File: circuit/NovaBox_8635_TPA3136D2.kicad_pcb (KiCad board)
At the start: 2 copper layers, 100 x 100 mm, 99 parts, among them P1 USB, P2 MH, P3 MH, P4 MH, P5 MH, Q1 IRLML6401, Q2 MMBT3904, Q3 IRLML6401, Q4 IRLML6344, Q5 MMBT3904, SW1 PIO18, SW2 PIO21, SW3 PIO8, SW4 PIO0, SW5 PIO1, SW6 ON/OFF, U1 CSR8635_MODULE, U2 CSR_DebugSmall, U3 TPA3136D2, U4 MCP6004

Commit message: mo powah pcb continued
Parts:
- removed C32: 1uF, NovaBox:C_0805
- removed L1, L3: 3.1A, NovaBox:R_0805
- removed SPK_LEFT1, SPK_RIGHT1: SPK, NovaBox:SPKR
- added L5: 3.1A, NovaBox:R_0805, F.Cu at (98.0, 122.0)
- added L6: 3.1A, NovaBox:R_0805, F.Cu at (90.5, 118.5)
- added R5: 10k, NovaBox:R_0805, F.Cu at (81.5, 104.0)
- added SPK1: SPK_L, NovaBox:SPKR, F.Cu at (114.0, 131.8)
- added SPK2: SPK_R, NovaBox:SPKR, F.Cu at (93.5, 132.5)
- C1: value 100uF -> 1uF; footprint NovaBox:CPOL_D10_P4.5 -> NovaBox:C_0805; moved to F.Cu
- C11, C24, C25: value 1nF -> 1uF
- C13, C22, C23, C27, C28, C6: value 1uF -> 1nF
- C14: value 220nF -> 1nF
- C15, C21: value 220nF -> 1uF
- C16: value 100nF -> 1uF
- C17: value 1uF -> 220nF
- C19, C20: value 1nF -> 220nF
- C2, C8: value 100nF -> 100uF; footprint NovaBox:C_0805 -> NovaBox:CPOL_D10_P4.5; moved to B.Cu
- C3, C5, C9: value 1nF -> 100nF
- C7: value 100uF -> 1nF; footprint NovaBox:CPOL_D10_P4.5 -> NovaBox:C_0805; moved to F.Cu
- Q2: value MMBT3904 -> IRLML6401
- Q3: value IRLML6401 -> MMBT3904
- Q4: value IRLML6344 -> MMBT3904
- Q5: value MMBT3904 -> IRLML6344
- R1: value 68 -> 1K
- R10: value 100k -> 10k
- R11: value 240K -> 68
- R12: value 620K -> 240K
- R13: value 68 -> 620K
- R17: value 240K -> 10K
- R18, R24: value 470K -> 10K
- R19: value 750 -> 240K
- R2: value 1K -> 68
- R21: value 270K -> 470K
- R22: value 10K -> 750
- R23: value 1K -> 270K
- R25: value 10K -> 470K
- R27: value 2K -> 1K
- R29: value 10K -> 2K
- R3: value 68 -> 10K
- R4, R8: value 10k -> 68
- R6: value 10K -> 100k; footprint NovaBox:R_0805 -> NovaBox:RPOT_RKT6V; moved to B.Cu
- R9: value 68 -> 100k
- moved C14 128.0 mm to (108.5, 132.0), turned to 180 degrees
- moved C18 127.1 mm to (101.5, 117.5), turned to 180 degrees
- moved C15 119.7 mm to (101.0, 99.5), turned to 270 degrees
- moved U3 116.9 mm to (99.5, 111.0), turned to 270 degrees
- moved R22 112.9 mm to (217.8, 86.8), turned to 180 degrees
- moved C1 112.7 mm to (223.0, 79.5)
- moved D7 107.3 mm to (217.8, 93.4), turned to 180 degrees
- moved C23 103.4 mm to (93.5, 127.5), turned to 270 degrees
- moved R16 102.4 mm to (205.0, 94.5), turned to 0 degrees
- moved C26 101.0 mm to (205.0, 92.5), turned to 0 degrees
- moved R15 101.0 mm to (205.0, 96.5), turned to 0 degrees
- moved C9 100.7 mm to (90.5, 113.5), turned to 270 degrees
- moved R24 98.8 mm to (217.8, 89.0)
- moved C10 98.1 mm to (92.5, 113.5), turned to 270 degrees
- moved R12 97.4 mm to (205.0, 103.5), turned to 0 degrees
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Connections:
- C1 pad 1: +BATT -> GND
- C1 pad 2: GND -> +BATT
- C10 pad 2: Net-(C10-Pad2) -> +BATT
- C11 pad 2: Net-(C10-Pad2) -> Net-(C11-Pad2)
- C12 pad 1: GND -> +5V
- C12 pad 2: Net-(C12-Pad2) -> GND
- C13 pad 1: Net-(C13-Pad1) -> GND
- C14 pad 2: Net-(C14-Pad2) -> Net-(C13-Pad2)
- C16 pad 1: CSR_RST -> GND
- C16 pad 2: GND -> Net-(C16-Pad2)
- C19 pad 1: GND -> Net-(C19-Pad1)
- C2 pad 1: GND -> +BATT
- C2 pad 2: +BATT -> GND
- C20 pad 2: Net-(C19-Pad2) -> Net-(C20-Pad2)
- C21 pad 2: Net-(C21-Pad2) -> GND
- C22 pad 1: Net-(C22-Pad1) -> GND
- C23 pad 2: Net-(C23-Pad2) -> Net-(C22-Pad2)
- C24 pad 1: GND -> Net-(C24-Pad1)
- C25 pad 2: Net-(C24-Pad2) -> Net-(C25-Pad2)
- C27 pad 1: Net-(C27-Pad1) -> GND
- C27 pad 2: GND -> Net-(C27-Pad2)
- C28 pad 2: GND -> Net-(C27-Pad2)
- C29 pad 1: +BATT -> Net-(C29-Pad1)
- C29 pad 2: Net-(C29-Pad2) -> GND
- C31 pad 1: +5V -> +BATT
- C31 pad 2: GND -> Net-(C31-Pad2)
- C4 pad 2: Net-(C4-Pad2) -> +BATT
- C5 pad 1: Net-(C5-Pad1) -> CSR_RST
- C5 pad 2: Net-(C4-Pad2) -> GND
- C6 pad 2: +BATT -> Net-(C6-Pad2)
- C7 pad 1: +BATT -> Net-(C7-Pad1)
- C7 pad 2: GND -> Net-(C6-Pad2)
- C8 pad 1: GND -> +BATT
- C8 pad 2: +BATT -> GND
- L2 pad 1: Net-(C10-Pad2) -> Net-(C6-Pad2)
- L2 pad 2: Net-(C15-Pad1) -> Net-(C17-Pad1)
- L4 pad 1: Net-(C24-Pad2) -> Net-(C13-Pad2)
- L4 pad 2: Net-(C21-Pad1) -> Net-(C18-Pad1)
- Q1 pad 2: GND -> VR_SHDN
- Q1 pad 3: Net-(Q1-Pad3) -> +BATT
- Q2 pad 3: PWER_E -> Net-(Q2-Pad3)
- Q3 pad 2: VR_SHDN -> GND
- Q3 pad 3: +BATT -> Net-(Q1-Pad1)
- Q4 pad 1: +BATT -> Net-(Q4-Pad1)
- Q4 pad 3: Net-(Q4-Pad3) -> PWER_E
- Q5 pad 1: Net-(Q5-Pad1) -> +BATT
- Q5 pad 3: Net-(Q3-Pad1) -> Net-(Q5-Pad3)
- R1 pad 1: Net-(C5-Pad1) -> 1V8
- R1 pad 2: GND -> Net-(R1-Pad2)
- R10 pad 1: Net-(R10-Pad1) -> +BATT
- R10 pad 2: +BATT -> Net-(Q2-Pad1)
- R11 pad 1: Net-(C26-Pad1) -> Net-(C28-Pad1)
- R11 pad 2: +BATT -> GND
- R12 pad 1: Net-(C26-Pad1) -> Net-(C21-Pad1)
- R12 pad 2: GND -> +BATT
- R13 pad 1: Net-(C25-Pad1) -> Net-(C21-Pad1)
- R14 pad 2: Net-(Q1-Pad3) -> Net-(Q2-Pad3)
- R15 pad 1: Net-(C27-Pad1) -> Net-(C26-Pad1)
- R16 pad 1: Net-(C27-Pad1) -> Net-(C26-Pad1)
- R17 pad 1: Net-(C28-Pad1) -> +BATT
- R17 pad 2: +BATT -> Net-(Q1-Pad1)
- R18 pad 1: Net-(C28-Pad1) -> Net-(Q3-Pad1)
- R18 pad 2: GND -> 1V8
- R19 pad 1: 2V5 -> Net-(C29-Pad1)
- R2 pad 1: 1V8 -> Net-(C7-Pad1)
- R2 pad 2: Net-(R2-Pad2) -> GND
- R20 pad 1: PWER_E -> VR_SHDN
- R20 pad 2: +BATT -> GND
- R21 pad 1: Net-(C30-Pad1) -> Net-(C29-Pad1)
- R21 pad 2: +BATT -> GND
- R22 pad 1: GND -> 2V5
- R22 pad 2: 2V5 -> +BATT
- R23 pad 1: Net-(Q2-Pad1) -> Net-(C30-Pad1)
- R23 pad 2: Net-(C29-Pad2) -> +BATT
- R24 pad 1: Net-(C30-Pad1) -> GND
- R24 pad 2: GND -> 2V5
- R25 pad 1: GND -> Net-(C30-Pad1)
- R25 pad 2: Net-(Q2-Pad1) -> GND
- R26 pad 1: +BATT -> PWER_E
- R26 pad 2: Net-(Q3-Pad1) -> +BATT
- R27 pad 1: Net-(Q4-Pad3) -> Net-(Q4-Pad1)
- R27 pad 2: Net-(D8-Pad2) -> Net-(C31-Pad2)
- R28 pad 1: Net-(Q5-Pad1) -> GND
- R28 pad 2: 1V8 -> Net-(Q4-Pad1)
- R29 pad 1: VR_SHDN -> Net-(Q5-Pad3)
- R29 pad 2: GND -> Net-(D8-Pad2)
- R3 pad 1: Net-(C11-Pad1) -> 1V8
- R3 pad 2: GND -> SPI_PCM
- R4 pad 1: (no net) -> Net-(C14-Pad1)
- R6 pad 1: 1V8 -> Net-(C16-Pad2)
- R6 pad 2: SPI_PCM -> Net-(R6-Pad2)
- R8 pad 1: +BATT -> Net-(C23-Pad1)
- R8 pad 2: Net-(Q1-Pad1) -> GND
- R9 pad 1: Net-(C20-Pad1) -> Net-(R9-Pad1)
- R9 pad 2: GND -> +BATT
- S1 pad 2: Net-(R10-Pad1) -> Net-(R9-Pad1)
- SW1 pad 2: Net-(R2-Pad2) -> Net-(R1-Pad2)
- SW2 pad 2: Net-(R2-Pad2) -> Net-(R1-Pad2)
- SW3 pad 2: Net-(R2-Pad2) -> Net-(R1-Pad2)
- SW4 pad 2: Net-(R2-Pad2) -> Net-(R1-Pad2)
- SW5 pad 2: Net-(R2-Pad2) -> Net-(R1-Pad2)
- SW6 pad 2: Net-(Q4-Pad3) -> Net-(Q5-Pad3)
- U1 pad 36: Net-(C22-Pad1) -> Net-(C25-Pad1)
- U1 pad 37: Net-(C23-Pad1) -> Net-(C24-Pad1)
- U1 pad 38: Net-(C17-Pad1) -> Net-(C15-Pad1)
- U1 pad 39: Net-(C13-Pad1) -> Net-(C11-Pad1)
- U3 pad 1: Net-(R10-Pad1) -> Net-(R9-Pad1)
- U3 pad 10: Net-(R5-Pad2) -> Net-(R6-Pad2)
- U3 pad 11: Net-(C22-Pad2) -> Net-(C25-Pad2)
- U3 pad 12: Net-(C23-Pad2) -> Net-(C24-Pad2)
- U3 pad 17: Net-(C21-Pad2) -> Net-(C20-Pad2)
- U3 pad 18: Net-(C21-Pad1) -> Net-(C20-Pad1)
- U3 pad 2: Net-(Q1-Pad1) -> Net-(Q2-Pad1)
- U3 pad 20: Net-(C18-Pad1) -> Net-(C19-Pad1)
- U3 pad 21: Net-(C18-Pad2) -> Net-(C19-Pad2)
- U3 pad 22: Net-(C15-Pad2) -> Net-(C18-Pad2)
- U3 pad 23: Net-(C15-Pad1) -> Net-(C18-Pad1)
- U3 pad 25: Net-(C14-Pad1) -> Net-(C17-Pad1)
- U3 pad 26: Net-(C14-Pad2) -> Net-(C17-Pad2)
- U3 pad 3: Net-(C13-Pad2) -> Net-(C11-Pad2)
- U3 pad 4: Net-(C17-Pad2) -> Net-(C15-Pad2)
- U3 pad 9: Net-(C12-Pad2) -> Net-(C16-Pad2)
- U4 pad 10: Net-(C28-Pad1) -> Net-(C29-Pad1)
- U4 pad 3: Net-(C26-Pad1) -> Net-(C21-Pad1)
- U4 pad 5: Net-(C27-Pad1) -> Net-(C26-Pad1)

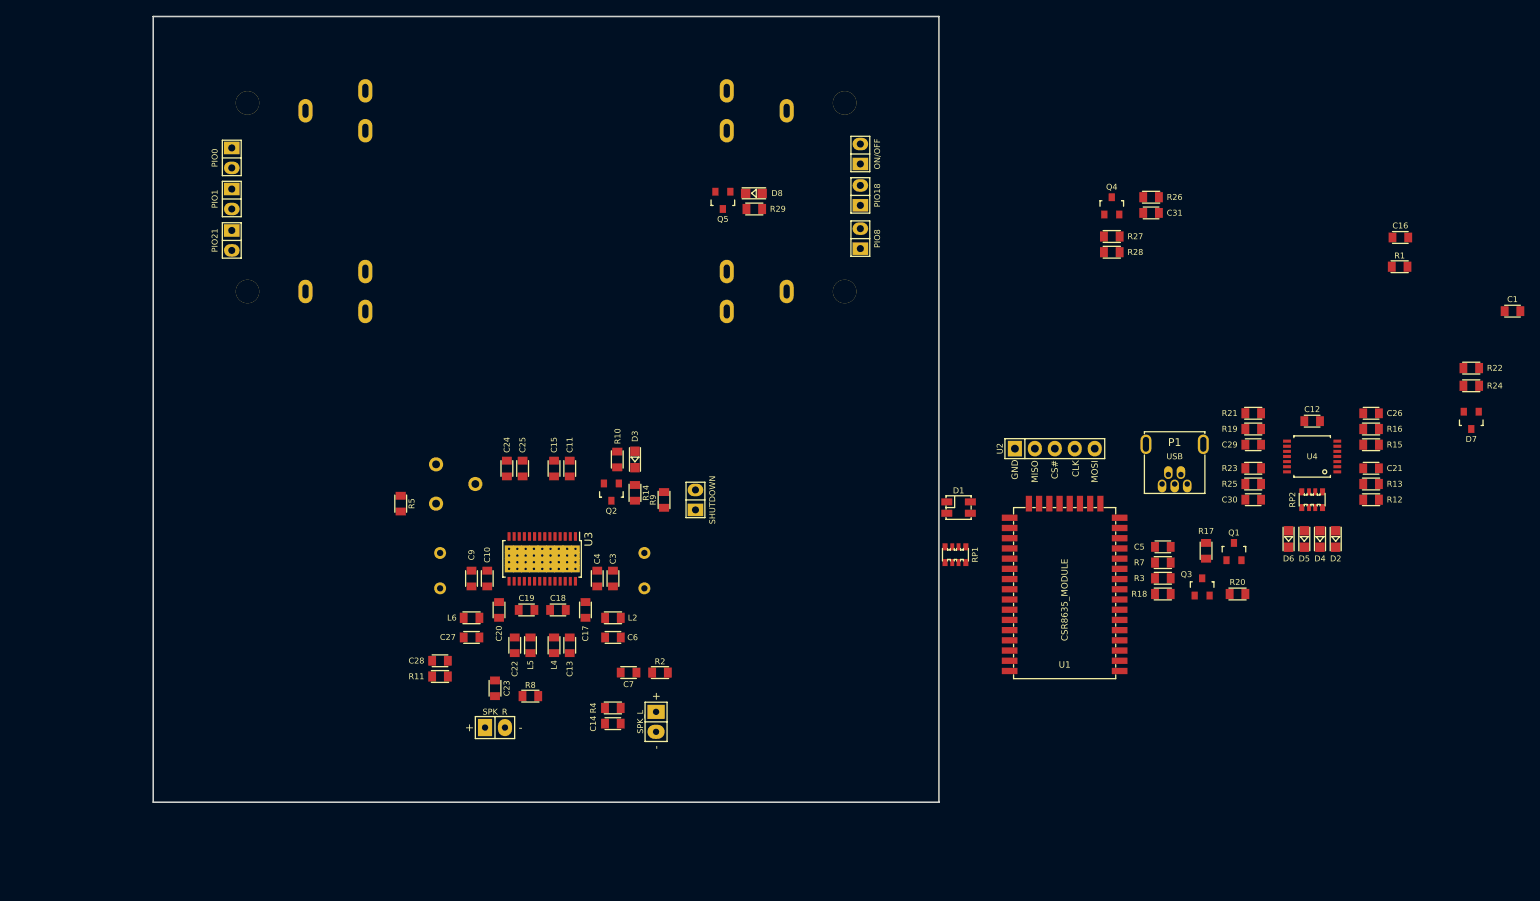
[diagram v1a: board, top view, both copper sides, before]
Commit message: changed power for two batteries; changed the opamp voltage resistor values
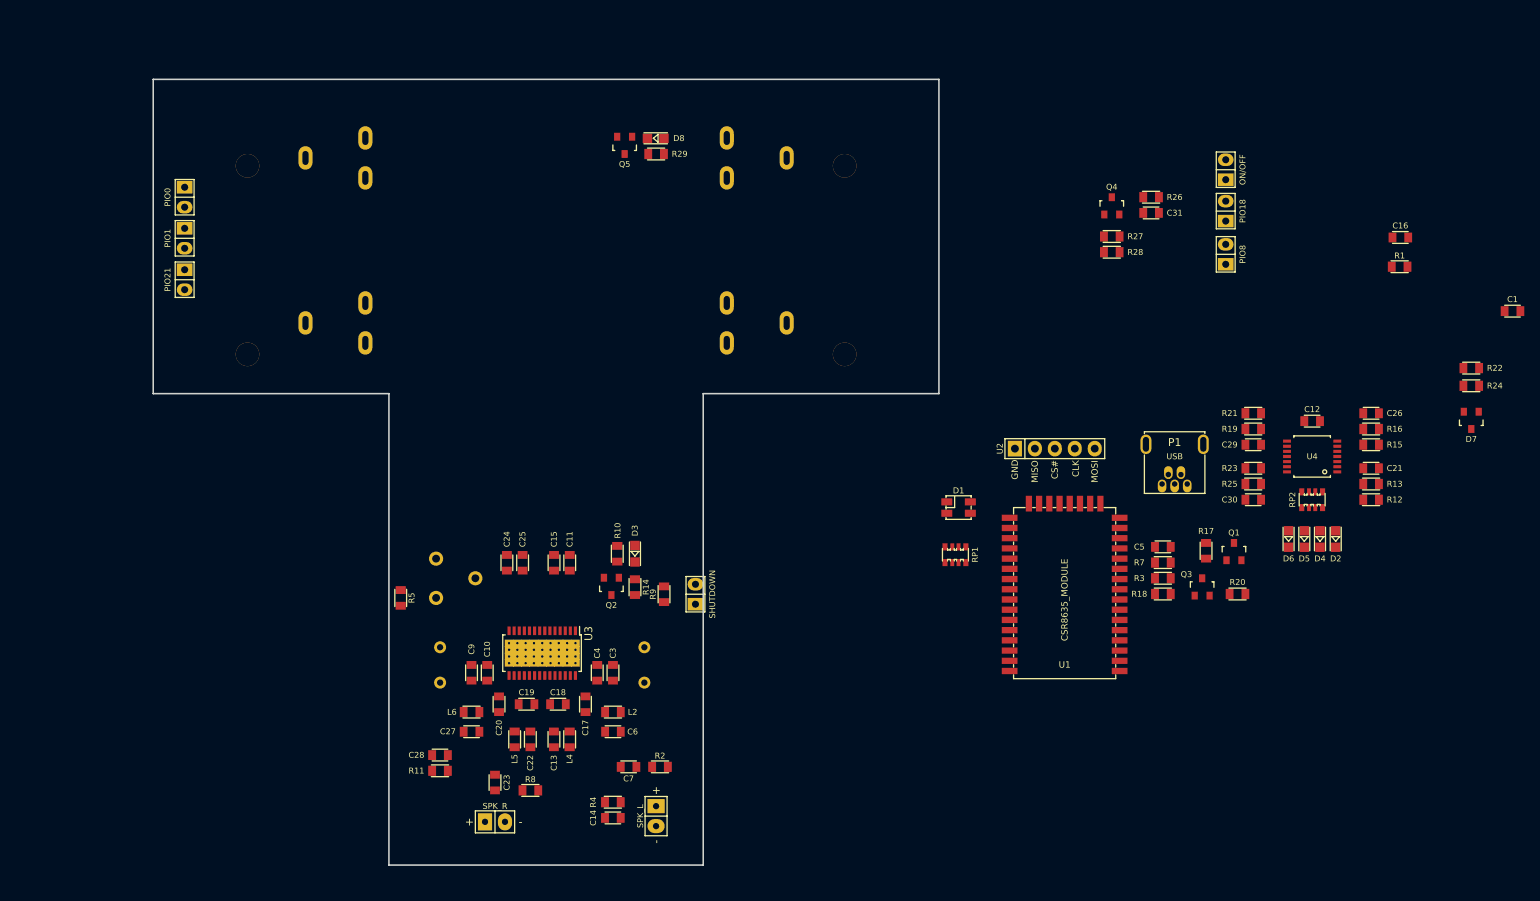
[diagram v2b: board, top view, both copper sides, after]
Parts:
- moved SW1 46.5 mm to (186.5, 66.8)
- moved SW3 46.5 mm to (186.5, 72.3)
- moved SW6 46.5 mm to (186.5, 61.5)
- moved P4 32.0 mm to (138.0, 85.0)
- moved P2 16.0 mm to (138.0, 61.0)
- moved D8 14.3 mm to (114.0, 57.5)
- moved Q5 14.3 mm to (110.0, 58.4)
- moved R29 14.3 mm to (114.0, 59.5)
- moved C13 12.1 mm to (101.0, 134.0)
- moved L5 12.1 mm to (96.0, 134.0)
- moved C22 12.1 mm to (98.0, 134.0)
- moved L4 12.1 mm to (103.0, 134.0)
- moved C10 12.0 mm to (92.5, 125.5)
- moved C11 12.0 mm to (103.0, 111.5)
- moved C14 12.0 mm to (108.5, 144.0)
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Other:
- outline, holes or cut-outs redrawn

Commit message: imported to pcb
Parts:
- removed D8: REVERSE_BATT, NovaBox:LED_0805
- removed R29: 2K, NovaBox:R_0805
- added C32: 1uF, NovaBox:C_0805, F.Cu at (205.5, 114.0)
- R12: value 240K -> 180K
- R13: value 620K -> 390K
- R15: value 270K -> 180K
- R16: value 620K -> 360K
- R19: value 240K -> 360K
- R21, R25: value 470K -> 680K
- R23: value 270K -> 390K
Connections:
- BT1 pad 1: Net-(BT1-Pad1) -> +4V
- BT2 pad 1: +BATT -> +8V
- BT2 pad 2: Net-(BT1-Pad1) -> +4V
- C1 pad 2: +BATT -> +8V
- C10 pad 2: +BATT -> +8V
- C12 pad 1: +5V -> +4V
- C2 pad 1: +BATT -> +8V
- C3 pad 2: +BATT -> +8V
- C31 pad 1: +BATT -> +4V
- C4 pad 2: +BATT -> +8V
- C8 pad 1: +BATT -> +8V
- C9 pad 2: +BATT -> +8V
- D1 pad 2: +BATT -> +4V
- D3 pad 2: +BATT -> +8V
- Q1 pad 2: VR_SHDN -> EN_DEVICES
- Q1 pad 3: +BATT -> +4V
- Q5 pad 1: +BATT -> +4V
- R10 pad 1: +BATT -> +8V
- R12 pad 2: +BATT -> +8V
- R15 pad 2: +BATT -> +8V
- R17 pad 1: +BATT -> +4V
- R19 pad 2: +BATT -> +8V
- R20 pad 1: VR_SHDN -> EN_DEVICES
- R22 pad 2: +BATT -> EN_DEVICES
- R23 pad 2: +BATT -> +8V
- R26 pad 2: +BATT -> +4V
- R9 pad 2: +BATT -> +8V
- U1 pad 27: +BATT -> +4V
- U3 pad 15: +BATT -> +8V
- U3 pad 16: +BATT -> +8V
- U3 pad 27: +BATT -> +8V
- U3 pad 28: +BATT -> +8V
- U3 pad 7: +BATT -> +8V
- U4 pad 4: +5V -> EN_DEVICES

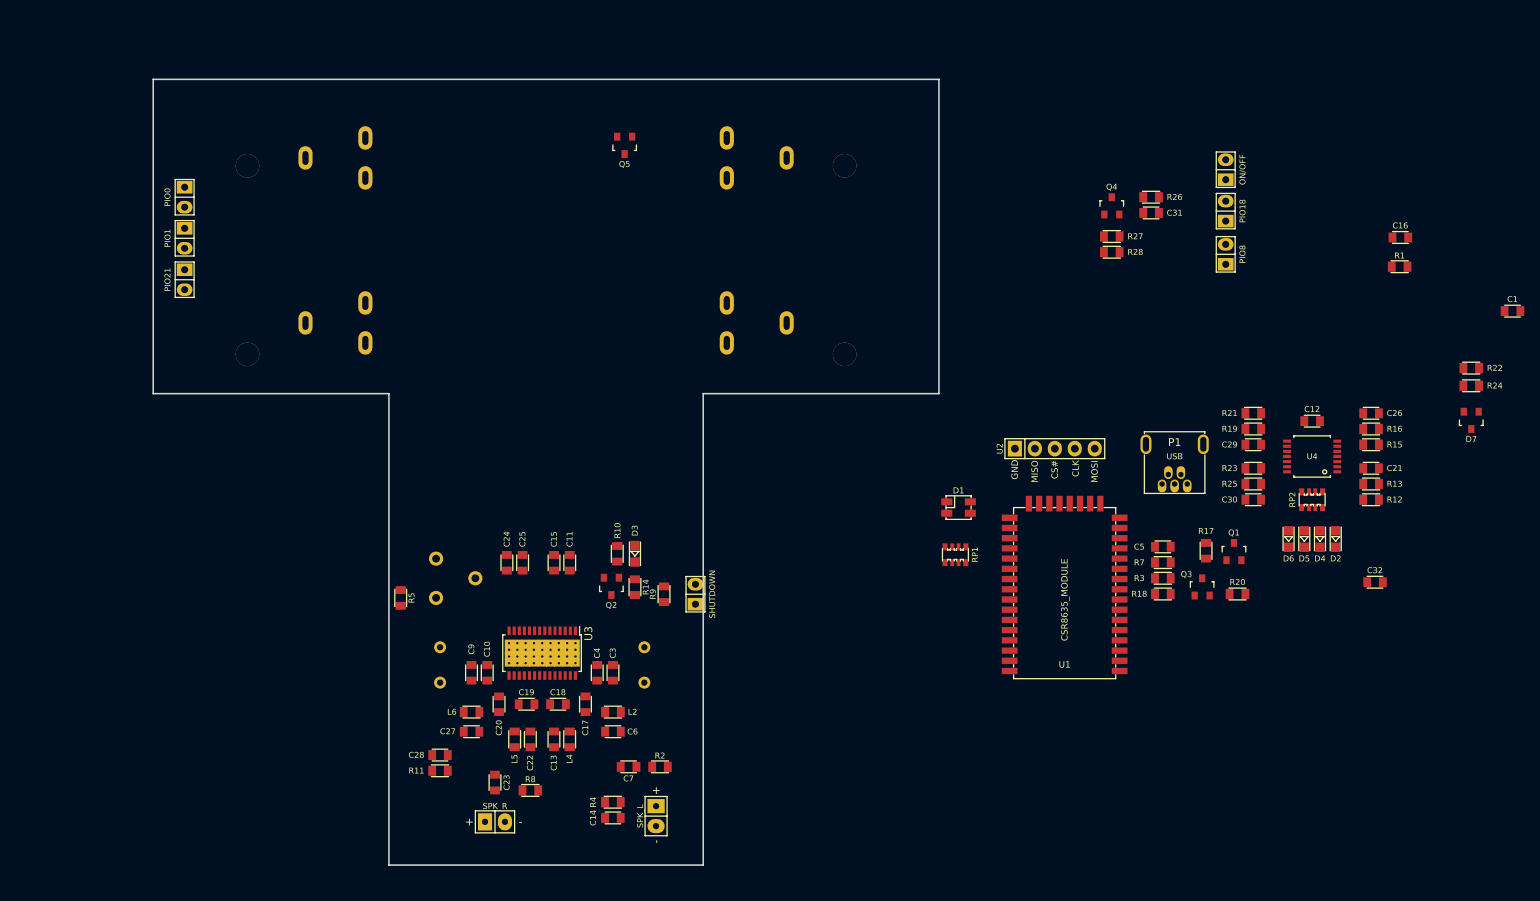
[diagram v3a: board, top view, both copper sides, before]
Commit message: more power started; pcb size for novabox!!
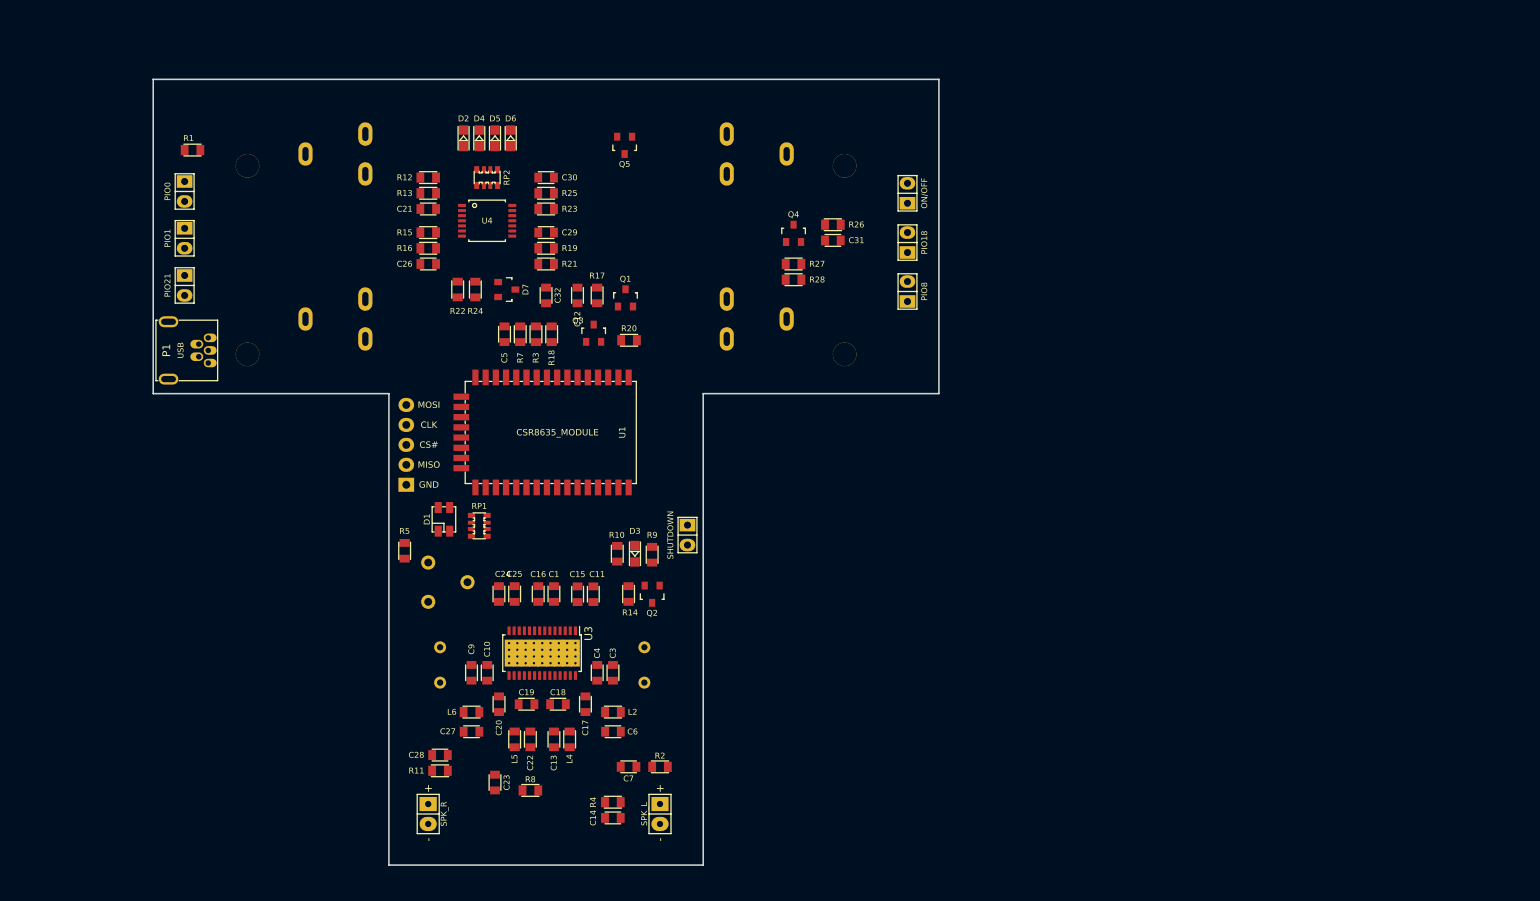
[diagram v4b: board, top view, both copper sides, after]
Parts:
- U2: moved to B.Cu
- moved R1 154.4 mm to (55.0, 59.0), turned to 180 degrees
- moved R22 129.4 mm to (88.8, 76.8), turned to 270 degrees
- moved R24 127.3 mm to (91.0, 76.8), turned to 90 degrees
- moved C1 127.2 mm to (101.0, 115.5), turned to 270 degrees
- moved R12 126.8 mm to (85.0, 62.5), turned to 180 degrees
- moved R13 125.6 mm to (85.0, 64.5), turned to 180 degrees
- moved C21 124.5 mm to (85.0, 66.5), turned to 180 degrees
- moved P1 124.2 mm to (57.0, 84.5), turned to 0 degrees
- moved D7 123.9 mm to (95.0, 76.8), turned to 270 degrees
- moved R15 123.0 mm to (85.0, 69.5), turned to 180 degrees
- moved R16 122.2 mm to (85.0, 71.5), turned to 180 degrees
- moved D2 122.2 mm to (89.5, 57.5), turned to 270 degrees
- moved C26 121.5 mm to (85.0, 73.5), turned to 180 degrees
- moved C16 118.7 mm to (99.0, 115.5), turned to 270 degrees
- moved D4 118.5 mm to (91.5, 57.5), turned to 270 degrees
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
